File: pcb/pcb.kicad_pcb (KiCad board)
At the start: 2 copper layers, 65 x 40 mm, 31 parts, among them J1 Conn_01x02, J2 Conn_01x06, J3 Load connect, J4 Screw_Terminal_01x02, K1 G5LE-1, Q1 2N7002, SW1 Reset, SW2 Flash, U1 RDM6300, U2 ESP-12E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

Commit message: Different optimizations
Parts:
- removed 2, 5, 6, h3: MountingHole_2.2mm_M2_Pad_Via, MountingHole:MountingHole_2.2mm_M2_Pad_Via
- added  : MountingHole_2.2mm_M2_Pad_Via, MountingHole:MountingHole_2.2mm_M2_Pad_Via, F.Cu at (-488.0, -363.0)
- added  : MountingHole_2.2mm_M2_Pad_Via, MountingHole:MountingHole_2.2mm_M2_Pad_Via, F.Cu at (-488.0, -397.0)
- added  : MountingHole_2.2mm_M2_Pad_Via, MountingHole:MountingHole_2.2mm_M2_Pad_Via, F.Cu at (-547.0, -397.0)
- added  : MountingHole_2.2mm_M2_Pad_Via, MountingHole:MountingHole_2.2mm_M2_Pad_Via, F.Cu at (-547.0, -363.0)
- added Q2: 2N7002, Package_TO_SOT_SMD:SOT-23, F.Cu at (-490.2, -386.3)
- added SW3: SW_DIP_x01, Connector_PinHeader_2.54mm:PinHeader_1x02_P2.54mm_Vertical, B.Cu at (-492.0, -393.9)
- J4: footprint TerminalBlock:TerminalBlock_bornier-2_P5.08mm -> TerminalBlock_TE-Connectivity:TerminalBlock_TE_282834-2_1x02_P2.54mm_Horizontal
- R1: value 400 -> 10k
- moved R4 29.6 mm to (-493.3, -386.1), turned to 270 degrees
- moved R7 23.2 mm to (-516.1, -376.8), turned to 270 degrees
- moved U3 15.8 mm to (-516.1, -382.0)
- moved R1 9.57 mm to (-488.4, -376.7)
- moved R6 6.48 mm to (-500.1, -368.3)
- moved REF** 5.75 mm to (-536.2, -388.0)
- moved C1 4.87 mm to (-513.3, -371.6), turned to 180 degrees
- moved R5 3.54 mm to (-492.0, -368.3), turned to 270 degrees
- moved BZ1 1.43 mm to (-491.6, -390.4)
- moved J4 1.00 mm to (-521.0, -364.0)
- renumbered SW2 to FLASH, SW1 to RESET
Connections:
- BZ1 pad 1: Net-(BZ1-Pad1) -> +3V3
- BZ1 pad 2: GND -> Net-(BZ1-Pad2)
- R1 pad 1: Net-(BZ1-Pad1) -> Net-(R1-Pad1)
- R1 pad 2: Net-(R1-Pad2) -> GND
- U2 pad 11: Net-(U2-Pad11) -> Net-(R6-Pad2)
- U2 pad 12: Net-(R1-Pad2) -> Net-(R5-Pad2)
- U2 pad 16: Net-(U2-Pad16) -> Net-(R1-Pad1)
- U2 pad 17: Net-(U2-Pad17) -> /BUZZER
- U2 pad 19: Net-(R6-Pad2) -> Net-(U2-Pad19)
- U2 pad 20: Net-(R5-Pad2) -> Net-(U2-Pad20)
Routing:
- net GND: track 138.2 -> 185.1 mm, vias 0 -> 5
- net Net-(R7-Pad1): track 35.0 -> 10.0 mm
- net Net-(R1-Pad2): track 24.8 -> 0.00 mm
- net Net-(BZ1-Pad2): track 0.00 -> 19.1 mm
- net Net-(J2-Pad3): track 54.5 -> 35.9 mm, vias 0 -> 2
- net Net-(R6-Pad2): track 30.7 -> 12.4 mm
- net +5V: track 86.9 -> 104.4 mm, vias 0 -> 1
- net Net-(J2-Pad4): track 38.2 -> 22.1 mm
- net +3V3: track 83.4 -> 98.7 mm, vias 0 -> 5
- net /RX: track 6.21 -> 19.6 mm
- net Net-(Q2-Pad3): track 0.00 -> 12.2 mm
- net /BUZZER: track 0.00 -> 10.5 mm
- net Net-(R1-Pad1): track 0.00 -> 9.97 mm
- net Net-(J2-Pad6): track 41.2 -> 50.1 mm
- net Net-(U2-Pad21): track 29.9 -> 21.6 mm
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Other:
- board text added: "PRISMO READER V2.0"

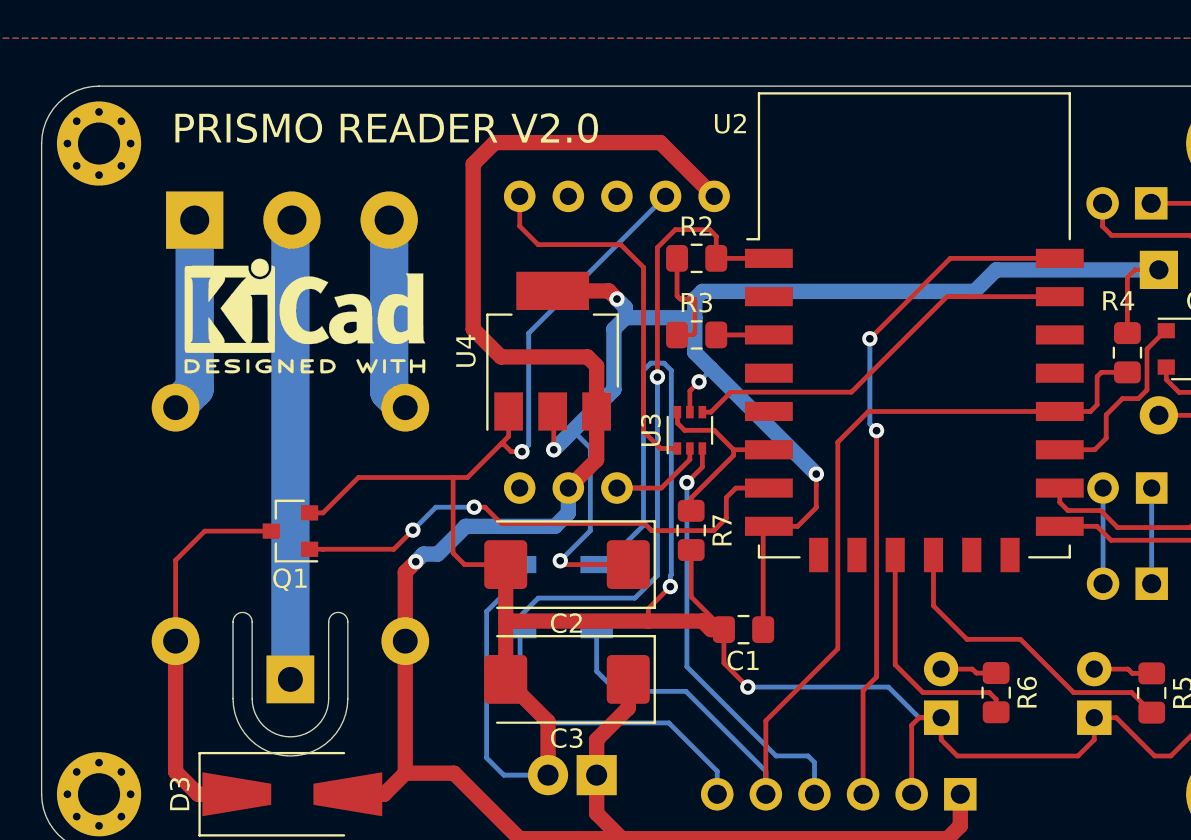
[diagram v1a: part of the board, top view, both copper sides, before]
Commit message: GPIO9 and GPIO10 should be not used, fix this
we cannot use these pins because they are internally connected to SPI
flash memory.
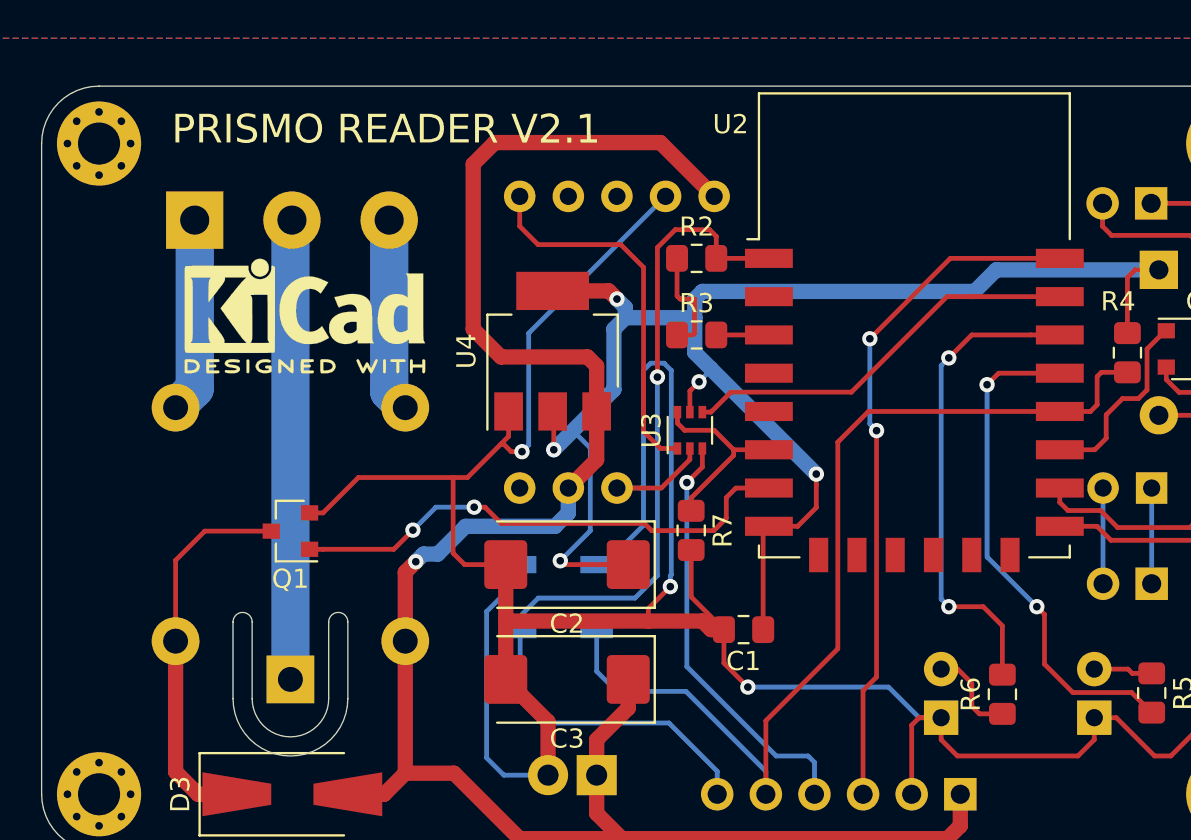
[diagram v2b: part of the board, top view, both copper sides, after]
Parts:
- moved R6 0.34 mm to (-499.8, -368.2), turned to 90 degrees
- renumbered RESET to SW1, FLASH to SW2
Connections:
- U2 pad 11: Net-(R6-Pad2) -> Net-(U2-Pad11)
- U2 pad 12: Net-(R5-Pad2) -> Net-(U2-Pad12)
- U2 pad 19: Net-(U2-Pad19) -> Net-(R5-Pad2)
- U2 pad 20: Net-(U2-Pad20) -> Net-(R6-Pad2)
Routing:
- net Net-(R6-Pad2): track 12.4 -> 25.4 mm, vias 0 -> 2
- net Net-(R5-Pad2): track 16.4 -> 26.5 mm, vias 0 -> 2
- net Net-(D2-Pad2): track 2.96 -> 4.87 mm
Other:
- board text added: "PRISMO READER V2.1"
- board text removed: "PRISMO READER V2.0"
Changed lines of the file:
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@@
     (thickness 1.6)
     (drawings 23)
-    (tracks 318)
+    (tracks 332)
     (zones 0)
     (modules 33)
@@
     (0 F.Cu signal)
     (31 B.Cu signal)
-    (32 B.Adhes user hide)
-    (33 F.Adhes user hide)
-    (34 B.Paste user hide)
-    (35 F.Paste user hide)
+    (32 B.Adhes user)
+    (33 F.Adhes user)
+    (34 B.Paste user)
+    (35 F.Paste user)
     (36 B.SilkS user)
     (37 F.SilkS user)
@@
   )
   (setup
-    (last_trace_width 0.8)
+    (last_trace_width 0.25)
     (user_trace_width 0.8)
     (user_trace_width 2)
@@
   (net 35 "Net-(R1-Pad1)")
   (net 36 /BUZZER)
-  (net 37 "Net-(U2-Pad19)")
-  (net 38 "Net-(U2-Pad20)")
+  (net 37 "Net-(U2-Pad11)")
+  (net 38 "Net-(U2-Pad12)")
   (net_class Default "This is the default net class."
     (clearance 0.2)
@@
     (add_net "Net-(U1-Pad8)")
     (add_net "Net-(U2-Pad10)")
+    (add_net "Net-(U2-Pad11)")
+    (add_net "Net-(U2-Pad12)")
     (add_net "Net-(U2-Pad13)")
     (add_net "Net-(U2-Pad14)")
-    (add_net "Net-(U2-Pad19)")
     (add_net "Net-(U2-Pad2)")
-    (add_net "Net-(U2-Pad20)")
     (add_net "Net-(U2-Pad21)")
     (add_net "Net-(U2-Pad4)")
@@
   )
   (module Resistor_SMD:R_0805_2012Metric_Pad1.15x1.40mm_HandSolder (layer F.Cu)
-    (at -500.126 -368.309 270)
+    (at -499.8 -368.225 90)
     (descr "Resistor SMD 0805 (2012 Metric), square (rectangular) end terminal, IPC_7351 nominal with elongated pad for handsoldering. (Body size source: https://docs.google.com/spreadsheets/d/1BsfQQcO9C6DZCsRaXUlFlo91Tg2WpOkGARC1WS5S8t0/edit?usp=sharing), generated with kicad-footprint-generator")
     (tags "resistor handsolder")
     (attr smd)
-    (fp_text reference R6 (at 0 -1.65 270) (layer F.SilkS)
-      (effects (font (size 1 1) (thickness 0.15)))
-    )
-    (fp_text value 200 (at 0 1.65 270) (layer F.Fab)
-      (effects (font (size 1 1) (thickness 0.15)))
-    )
-    (fp_text user %R (at 0 0 270) (layer F.Fab)
+    (fp_text reference R6 (at 0 -1.65 90) (layer F.SilkS)
+      (effects (font (size 1 1) (thickness 0.15)))
+    )
+    (fp_text value 200 (at 0 1.65 90) (layer F.Fab)
+      (effects (font (size 1 1) (thickness 0.15)))
+    )
+    (fp_text user %R (at 0 0 90) (layer F.Fab)
       (effects (font (size 0.5 0.5) (thickness 0.08)))
     )
@@
     (fp_line (start -1 -0.6) (end 1 -0.6) (layer F.Fab) (width 0.1))
     (fp_line (start -1 0.6) (end -1 -0.6) (layer F.Fab) (width 0.1))
-    (pad 2 smd roundrect (at 1.025 0 270) (size 1.15 1.4) (layers F.Cu F.Paste F.Mask) (roundrect_rratio 0.217391)
+    (pad 2 smd roundrect (at 1.025 0 90) (size 1.15 1.4) (layers F.Cu F.Paste F.Mask) (roundrect_rratio 0.217391)
       (net 19 "Net-(R6-Pad2)"))
-    (pad 1 smd roundrect (at -1.025 0 270) (size 1.15 1.4) (layers F.Cu F.Paste F.Mask) (roundrect_rratio 0.217391)
+    (pad 1 smd roundrect (at -1.025 0 90) (size 1.15 1.4) (layers F.Cu F.Paste F.Mask) (roundrect_rratio 0.217391)
       (net 5 "Net-(D2-Pad2)"))
     (model ${KISYS3DMOD}/Resistor_SMD.3dshapes/R_0805_2012Metric.wrl
@@
     (tags "Tactile Switch")
     (attr smd)
-    (fp_text reference RESET (at 4.05 0.75) (layer B.SilkS)
+    (fp_text reference SW1 (at 4.05 0.75) (layer B.SilkS)
       (effects (font (size 1 1) (thickness 0.15)) (justify mirror))
     )
@@
     (tags "Tactile Switch")
     (attr smd)
-    (fp_text reference FLASH (at -4.05 1 180) (layer B.SilkS)
+    (fp_text reference SW2 (at -4.05 1 180) (layer B.SilkS)
       (effects (font (size 1 1) (thickness 0.15)) (justify mirror))
     )
@@
       (net 29 "Net-(U2-Pad10)"))
     (pad 11 smd rect (at -1 12) (size 1 1.8) (layers F.Cu F.Paste F.Mask)
-      (net 19 "Net-(R6-Pad2)"))
+      (net 37 "Net-(U2-Pad11)"))
     (pad 12 smd rect (at 1 12) (size 1 1.8) (layers F.Cu F.Paste F.Mask)
-      (net 18 "Net-(R5-Pad2)"))
+      (net 38 "Net-(U2-Pad12)"))
     (pad 13 smd rect (at 3 12) (size 1 1.8) (layers F.Cu F.Paste F.Mask)
       (net 30 "Net-(U2-Pad13)"))
@@
       (net 11 "Net-(J2-Pad5)"))
     (pad 19 smd rect (at 7.6 2.5) (size 2.5 1) (layers F.Cu F.Paste F.Mask)
-      (net 37 "Net-(U2-Pad19)"))
+      (net 18 "Net-(R5-Pad2)"))
     (pad 20 smd rect (at 7.6 0.5) (size 2.5 1) (layers F.Cu F.Paste F.Mask)
-      (net 38 "Net-(U2-Pad20)"))
+      (net 19 "Net-(R6-Pad2)"))
     (pad 21 smd rect (at 7.6 -1.5) (size 2.5 1) (layers F.Cu F.Paste F.Mask)
       (net 32 "Net-(U2-Pad21)"))
@@
       (xy -2.9464 -2.607733) (xy -2.9464 -2.510946)) (layer F.SilkS) (width 0.01))
   )
-  (gr_text "PRISMO READER V2.0" (at -532 -397.75) (layer F.SilkS)
+  (gr_text "PRISMO READER V2.1" (at -532 -397.75) (layer F.SilkS)
     (effects (font (size 1.5 1.5) (thickness 0.15)))
   )
@@
   (segment (start -493.014 -369.316) (end -491.998 -369.316) (width 0.25) (layer F.Cu) (net 4))
   (segment (start -493.238 -369.54) (end -493.014 -369.316) (width 0.25) (layer F.Cu) (net 4))
-  (segment (start -503 -369.54) (end -501.366 -369.54) (width 0.25) (layer F.Cu) (net 5))
-  (segment (start -501.16 -369.334) (end -500.126 -369.334) (width 0.25) (layer F.Cu) (net 5))
-  (segment (start -501.366 -369.54) (end -501.16 -369.334) (width 0.25) (layer F.Cu) (net 5))
+  (segment (start -503 -369.54) (end -502.14 -369.54) (width 0.25) (layer F.Cu) (net 5))
+  (segment (start -502.14 -369.54) (end -501.4 -368.8) (width 0.25) (layer F.Cu) (net 5))
+  (segment (start -501.4 -368.8) (end -501.4 -367.6) (width 0.25) (layer F.Cu) (net 5))
+  (segment (start -501 -367.2) (end -499.8 -367.2) (width 0.25) (layer F.Cu) (net 5))
+  (segment (start -501.4 -367.6) (end -501 -367.2) (width 0.25) (layer F.Cu) (net 5))
   (segment (start -538 -376.75) (end -541.475 -376.75) (width 0.25) (layer F.Cu) (net 6))
   (segment (start -543 -375.225) (end -543 -371) (width 0.25) (layer F.Cu) (net 6))
@@
   (segment (start -493.046999 -368.314999) (end -496.076999 -368.314999) (width 0.25) (layer F.Cu) (net 18))
   (segment (start -491.998 -367.266) (end -493.046999 -368.314999) (width 0.25) (layer F.Cu) (net 18))
-  (segment (start -496.076999 -368.314999) (end -498.856 -371.094) (width 0.25) (layer F.Cu) (net 18))
-  (segment (start -498.856 -371.094) (end -501.65 -371.094) (width 0.25) (layer F.Cu) (net 18))
-  (segment (start -503.4 -372.844) (end -503.4 -375.5) (width 0.25) (layer F.Cu) (net 18))
-  (segment (start -501.65 -371.094) (end -503.4 -372.844) (width 0.25) (layer F.Cu) (net 18))
-  (segment (start -500.126 -367.959) (end -500.126 -367.284) (width 0.25) (layer F.Cu) (net 19))
-  (segment (start -500.481999 -368.314999) (end -500.126 -367.959) (width 0.25) (layer F.Cu) (net 19))
-  (segment (start -503.950999 -368.314999) (end -500.481999 -368.314999) (width 0.25) (layer F.Cu) (net 19))
-  (segment (start -505.4 -369.764) (end -503.950999 -368.314999) (width 0.25) (layer F.Cu) (net 19))
-  (segment (start -505.4 -375.5) (end -505.4 -369.764) (width 0.25) (layer F.Cu) (net 19))
+  (segment (start -496.076999 -368.314999) (end -496.114999 -368.314999) (width 0.25) (layer F.Cu) (net 18))
+  (segment (start -496.114999 -368.314999) (end -497.6 -369.8) (width 0.25) (layer F.Cu) (net 18))
+  (via (at -498 -372.8) (size 0.8) (drill 0.4) (layers F.Cu B.Cu) (net 18))
+  (segment (start -497.6 -372.4) (end -498 -372.8) (width 0.25) (layer F.Cu) (net 18))
+  (segment (start -497.6 -369.8) (end -497.6 -372.4) (width 0.25) (layer F.Cu) (net 18))
+  (via (at -500.6 -384.4) (size 0.8) (drill 0.4) (layers F.Cu B.Cu) (net 18))
+  (segment (start -500.6 -375.4) (end -500.6 -384.4) (width 0.25) (layer B.Cu) (net 18))
+  (segment (start -498 -372.8) (end -500.6 -375.4) (width 0.25) (layer B.Cu) (net 18))
+  (segment (start -500 -385) (end -496.8 -385) (width 0.25) (layer F.Cu) (net 18))
+  (segment (start -500.6 -384.4) (end -500 -385) (width 0.25) (layer F.Cu) (net 18))
+  (segment (start -496.8 -387) (end -498.3 -387) (width 0.25) (layer F.Cu) (net 19))
+  (via (at -502.6 -385.8) (size 0.8) (drill 0.4) (layers F.Cu B.Cu) (net 19))
+  (segment (start -501.4 -387) (end -502.6 -385.8) (width 0.25) (layer F.Cu) (net 19))
+  (segment (start -498.3 -387) (end -501.4 -387) (width 0.25) (layer F.Cu) (net 19))
+  (segment (start -502.6 -385.8) (end -503 -385.4) (width 0.25) (layer B.Cu) (net 19))
+  (via (at -502.6 -372.8) (size 0.8) (drill 0.4) (layers F.Cu B.Cu) (net 19))
+  (segment (start -503 -373.2) (end -502.6 -372.8) (width 0.25) (layer B.Cu) (net 19))
+  (segment (start -503 -385.4) (end -503 -373.2) (width 0.25) (layer B.Cu) (net 19))
+  (segment (start -499.8 -369.25) (end -499.8 -371.8) (width 0.25) (layer F.Cu) (net 19))
+  (segment (start -500.8 -372.8) (end -502.6 -372.8) (width 0.25) (layer F.Cu) (net 19))
+  (segment (start -499.8 -371.8) (end -500.8 -372.8) (width 0.25) (layer F.Cu) (net 19))
   (segment (start -516.778 -382.391) (end -516.403 -382.016) (width 0.25) (layer F.Cu) (net 20))
   (segment (start -516.778 -382.966) (end -516.778 -382.391) (width 0.25) (layer F.Cu) (net 20))

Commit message: Move to ESP32 and Gwiot7941e reader
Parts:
- D1 BLUE: renamed from D1
- D2 RED: renamed from D2
- moved C1 811.3 mm to (141.5, 107.4)
- moved R6 811.3 mm to (155.0, 110.8)
- moved U3 811.3 mm to (138.7, 97.0)
- moved   811.3 mm to (166.8, 116.0)
- moved   811.3 mm to (166.8, 82.0)
- moved   811.3 mm to (107.8, 82.0)
- moved   811.3 mm to (107.8, 116.0)
- moved BZ1 811.3 mm to (163.2, 88.6)
- moved C2 811.3 mm to (132.2, 104.0)
- moved C3 811.3 mm to (132.2, 110.0)
- moved D1 BLUE 811.3 mm to (159.8, 112.0)
- moved D2 RED 811.3 mm to (151.8, 112.0)
- moved D3 811.3 mm to (117.9, 116.0)
- moved FLASH 811.3 mm to (133.8, 105.7)
- moved J1 811.3 mm to (162.8, 105.0)
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- renumbered SW2 to FLASH, SW1 to RESET
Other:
- net class Default removed
- board text added: "+"
- board text added: "-"
- board text added: "AAA"
- board text added: "PRISMO READER V2.2"
- board text removed: "PRISMO READER V2.1"
